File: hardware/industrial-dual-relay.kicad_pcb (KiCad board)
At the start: 2 copper layers, 40 x 40 mm, 34 parts, among them P1 CON-SENSOR2, P2 BOOT, P3 CONN_8, P4 Debug, Q1 SSM6N7002KFU, U1 XMC1100, U2 G5LE-1-36, U3 G5LE-1-36, U4 DRILL, U5 DRILL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

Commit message: move to kicad 6, fix schematic library links
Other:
- net class Default removed

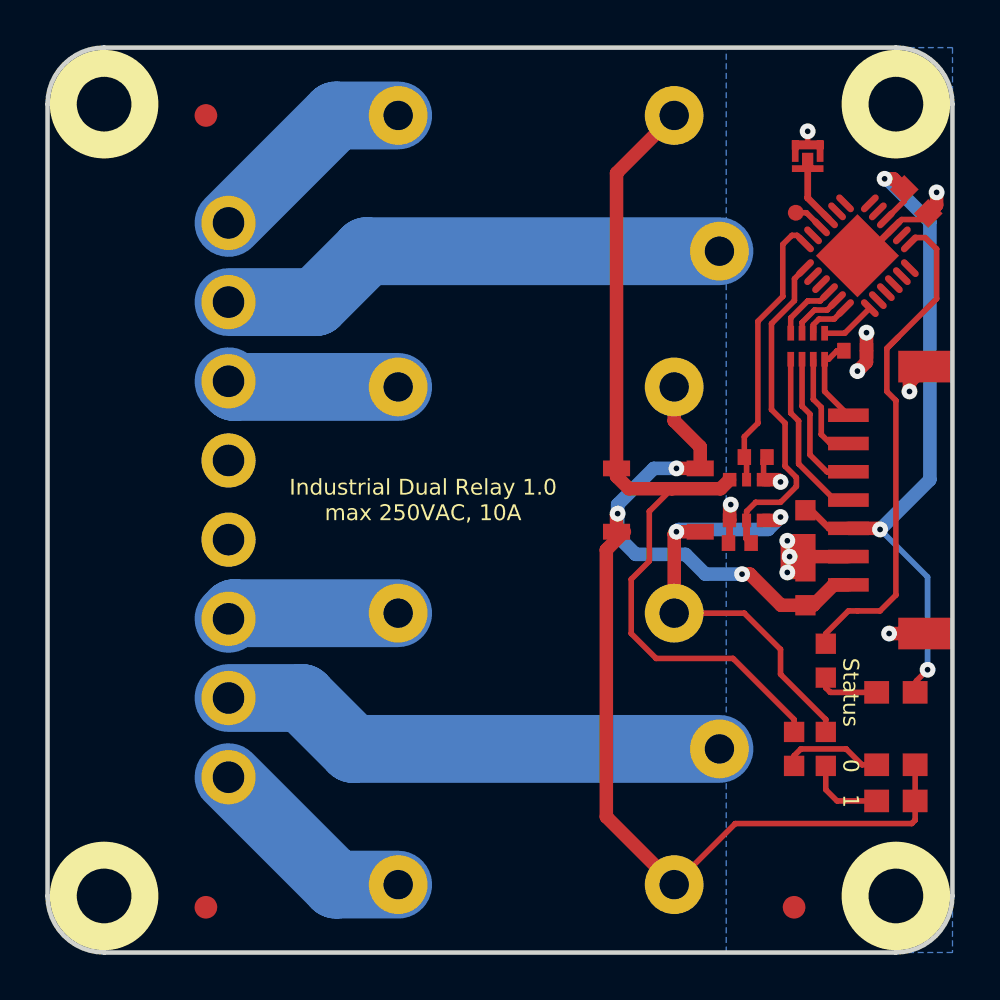
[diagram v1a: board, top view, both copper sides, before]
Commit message: Version 1.1: changed relay, more clearance
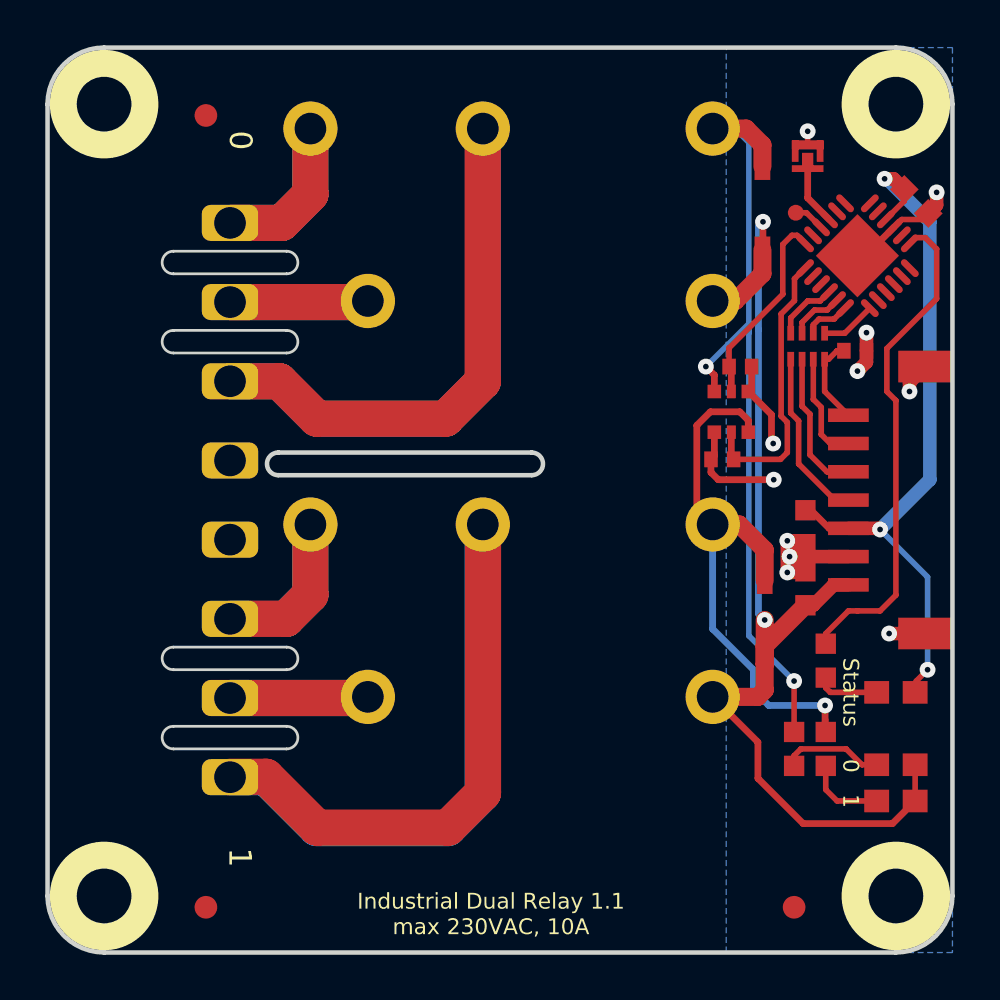
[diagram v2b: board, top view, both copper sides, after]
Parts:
- removed U2, U3: G5LE-1-36, kicad-libraries:G5LE-1
- added Q2: G5Q-1, kicad-libraries:G5Q-1, F.Cu at (161.5, 95.4)
- added Q3: G5Q-1, kicad-libraries:G5Q-1, F.Cu at (161.5, 112.9)
- P3: footprint kicad-libraries:OQ_8P -> kicad-libraries:OQ_8P_230V
- moved D4 12.4 mm to (163.7, 91.3), turned to -90 degrees
- moved D5 6.17 mm to (163.8, 109.6), turned to -90 degrees
- moved VAL 5.68 mm to (153.5, 98.7)
- moved R5 4.06 mm to (162.7, 98.3)
- moved locked 3.96 mm to (162.3, 100.3)
- moved R4 3.78 mm to (161.9, 102.4)
- moved VAL 2.19 mm to (153.7, 92.7)
- moved G*** 1.63 mm to (153.7, 113.9)
- moved P3 0.07 mm to (140.1, 104.2)
- renumbered Q1 to locked
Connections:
- P3 pad 4: (no net) -> unconnected-(P3-Pad4)
- P3 pad 5: (no net) -> unconnected-(P3-Pad5)
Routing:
- net Net-(P3-Pad3): track 7.60 -> 47.4 mm
- net Net-(P3-Pad8): track 9.47 -> 49.2 mm
- net Net-(P3-Pad7): track 22.6 -> 12.2 mm
- net Net-(P3-Pad2): track 22.6 -> 12.2 mm
- net Net-(P3-Pad6): track 7.60 -> 14.2 mm
- net +5V: track 53.9 -> 48.2 mm, vias 3 -> 2
- net GND: track 28.7 -> 33.7 mm
- net Net-(P3-Pad1): track 9.47 -> 14.0 mm
- net RELAY0: track 12.4 -> 8.82 mm
- net RELAY1: track 14.9 -> 12.4 mm
- net Net-(D4-Pad1): track 38.9 -> 36.5 mm, vias 0 -> 2
- net Net-(D5-Pad1): track 24.4 -> 25.2 mm, vias 2 -> 1
- net Net-(R1-Pad1): track 22.8 -> 22.1 mm
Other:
- outline, holes or cut-outs redrawn
- board text added: "COM"
- board text added: "Industrial Dual Relay 1.1 max 230VAC, 10A"
- board text added: "NC"
- board text added: "NO"
- board text added: "X"
- board text removed: "A"
- board text removed: "B"
- board text removed: "Industrial Dual Relay 1.0 max 250VAC, 10A"
- board text removed: "S"

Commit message: updated diode to minimelf footprint
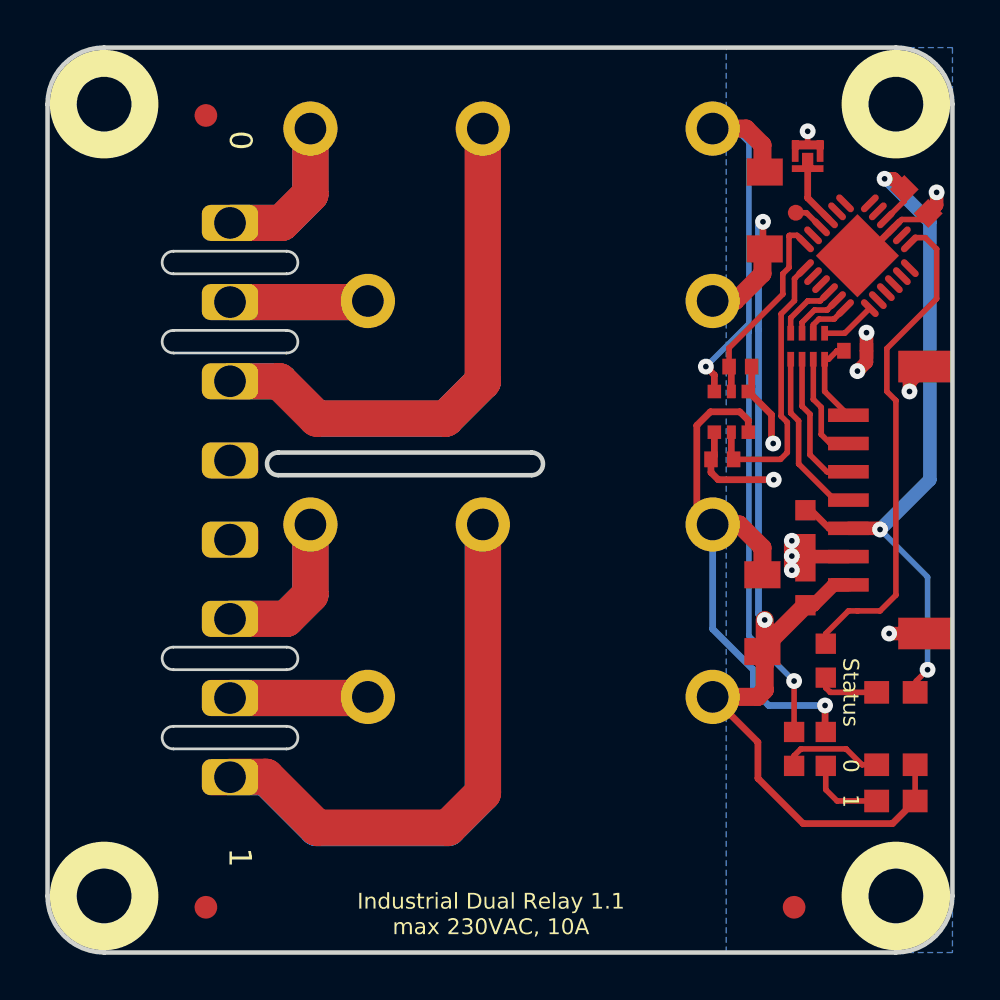
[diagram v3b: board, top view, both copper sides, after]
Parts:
- D4, D5: footprint kicad-libraries:SOD-123 -> kicad-libraries:MiniMelf
- moved D5 0.41 mm to (163.7, 109.2), turned to 90 degrees
- moved D4 0.14 mm to (163.8, 91.4), turned to 90 degrees
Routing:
- net Net-(D5-Pad1): track 25.2 -> 24.4 mm
- net GND: track 33.7 -> 33.1 mm
